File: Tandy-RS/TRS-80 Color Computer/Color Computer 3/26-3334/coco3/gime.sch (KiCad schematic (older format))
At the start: 28 parts, among them IC10 74LS244, IC11 74LS244, IC12 74LS244, IC13 74LS374, IC15 74LS04, IC6 TCC1014, IC9 74LS138, X1 Crystal

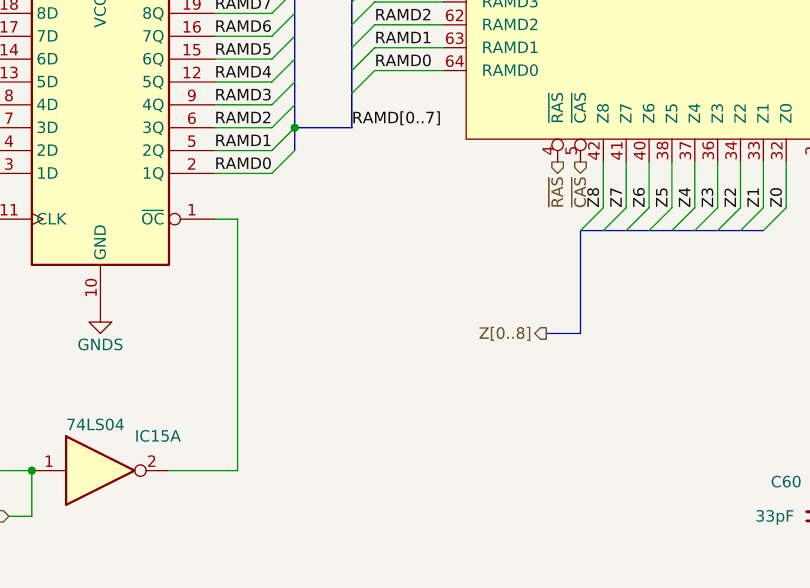
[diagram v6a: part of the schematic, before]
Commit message: found and added lost capacitor c68
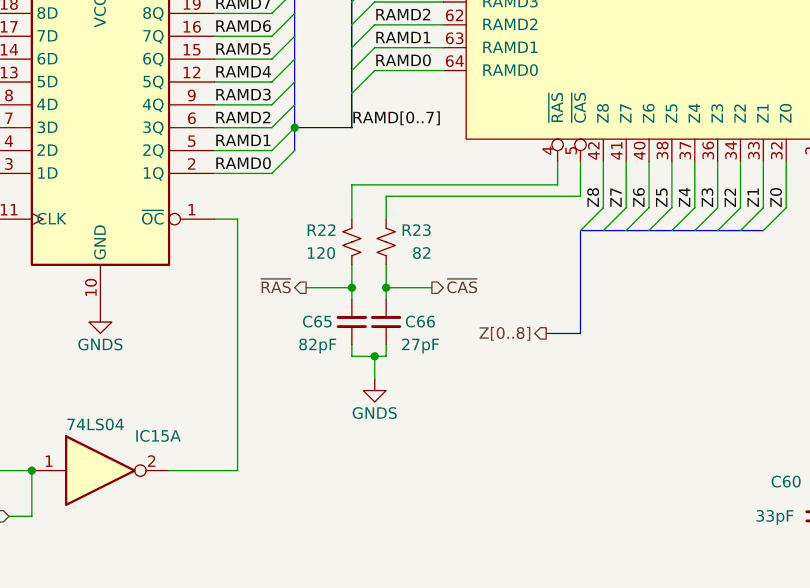
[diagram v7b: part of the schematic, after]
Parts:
- added C65: 82pF, Capacitor_THT:C_Rect_L7.2mm_W3.0mm_P5.00mm_FKS2_FKP2_MKS2_MKP2, symbol Device:C_Small
- added C66: 27pF, Capacitor_THT:C_Rect_L7.2mm_W3.0mm_P5.00mm_FKS2_FKP2_MKS2_MKP2, symbol Device:C_Small
- added R22: 120, Resistor_THT:R_Axial_DIN0207_L6.3mm_D2.5mm_P10.16mm_Horizontal, symbol Device:R_Small_US
- added R23: 82, Resistor_THT:R_Axial_DIN0207_L6.3mm_D2.5mm_P10.16mm_Horizontal, symbol Device:R_Small_US
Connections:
- net GNDS: now also C65.1, C66.1
- net ~CAS: now also C66.2, R23.1; no longer IC6.5 (~CAS)
- net ~RAS: now also C65.2, R22.1; no longer IC6.4 (~RAS)
- new net: IC6.4 (~RAS), R22.2
- new net: IC6.5 (~CAS), R23.2
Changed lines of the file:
@@
 Wire Wire Line
 	4150 6750 4450 6750
-Text HLabel 6850 5400 3    50   Output ~ 0
+Text HLabel 6200 5950 2    50   Output ~ 0
 ~CAS
-Text HLabel 6750 5400 3    50   Output ~ 0
+Text HLabel 5650 5950 0    50   Output ~ 0
 ~RAS
 Text HLabel 4350 6950 0    50   Input ~ 0
@@
 Text Label 6000 4000 0    50   ~ 0
 ~WE1
-Wire Bus Line
-	1950 2200 1950 5950
-Wire Bus Line
-	6100 2150 8050 2150
-Wire Bus Line
-	5900 850  5900 3500
-Wire Bus Line
-	6850 5700 7650 5700
-Wire Bus Line
-	3900 4850 3900 6950
-Wire Bus Line
-	3650 4850 3650 6950
-Wire Bus Line
-	3900 850  3900 2700
-Wire Bus Line
-	3650 850  3650 2700
-Wire Bus Line
-	5850 4400 5850 5250
-Wire Bus Line
-	5600 2200 5600 5250
 Text HLabel 5900 4000 0    50   Output ~ 0
 ~WE1
+$Comp
+L Device:R_Small_US R?
+U 1 1 612F6A83
+P 5850 5750
+AR Path="/60273794/612F6A83" Ref="R?"  Part="1"
+AR Path="/603D560B/612F6A83" Ref="R?"  Part="1"
+AR Path="/603CF7B8/612F6A83" Ref="R?"  Part="1"
+AR Path="/612A4892/612F6A83" Ref="R?"  Part="1"
+AR Path="/61257512/612F6A83" Ref="R22"  Part="1"
+F 0 "R22" H 5650 5700 50  0000 L CNN
+F 1 " 120" H 5650 5800 50  0000 L CNN
+F 2 "Resistor_THT:R_Axial_DIN0207_L6.3mm_D2.5mm_P10.16mm_Horizontal" H 5850 5750 50  0001 C CNN
+F 3 " https://www.seielect.com/catalog/sei-cf_cfm.pdf" H 5850 5750 50  0001 C CNN
+F 4 "digikey" H 5850 5750 50  0001 C CNN "Vendor"
+F 5 "CF14JT120RCT-ND" H 5850 5750 50  0001 C CNN "Vendor part#"
+F 6 "CF14JT120R" H 5850 5750 50  0001 C CNN "Manufacturer part#"
+	1    5850 5750
+	1    0    0    1
+$EndComp
+Wire Wire Line
+	6750 5400 6750 5500
+Wire Wire Line
+	6750 5500 5850 5500
+Wire Wire Line
+	5850 5500 5850 5650
+$Comp
+L Device:R_Small_US R?
+U 1 1 61342388
+P 6000 5750
+AR Path="/60273794/61342388" Ref="R?"  Part="1"
+AR Path="/603D560B/61342388" Ref="R?"  Part="1"
+AR Path="/603CF7B8/61342388" Ref="R?"  Part="1"
+AR Path="/612A4892/61342388" Ref="R?"  Part="1"
+AR Path="/61257512/61342388" Ref="R23"  Part="1"
+F 0 "R23" H 5800 5700 50  0000 L CNN
+F 1 "82" H 5800 5800 50  0000 L CNN
+F 2 "Resistor_THT:R_Axial_DIN0207_L6.3mm_D2.5mm_P10.16mm_Horizontal" H 6000 5750 50  0001 C CNN
+F 3 "https://www.koaspeer.com/pdfs/CF.pdf" H 6000 5750 50  0001 C CNN
+F 4 "digikey" H 6000 5750 50  0001 C CNN "Vendor"
+F 5 "2019-CF1/4CT52R820JCT-ND" H 6000 5750 50  0001 C CNN "Vendor part#"
+F 6 "CF1/4CT52R820J" H 6000 5750 50  0001 C CNN "Manufacturer part#"
+	1    6000 5750
+	-1   0    0    1
+$EndComp
+Wire Wire Line
+	6850 5400 6850 5550
+Wire Wire Line
+	6850 5550 6000 5550
+Wire Wire Line
+	6000 5550 6000 5650
+$Comp
+L Device:C_Small C?
+U 1 1 6136F6EC
+P 6000 6100
+AR Path="/60273794/6136F6EC" Ref="C?"  Part="1"
+AR Path="/602A51A8/6136F6EC" Ref="C?"  Part="1"
+AR Path="/603CF7B8/6136F6EC" Ref="C?"  Part="1"
+AR Path="/61257512/6136F6EC" Ref="C66"  Part="1"
+F 0 "C66" H 5850 6100 50  0000 C CNN
+F 1 "27pF" H 5850 6200 50  0000 C CNN
+F 2 "Capacitor_THT:C_Rect_L7.2mm_W3.0mm_P5.00mm_FKS2_FKP2_MKS2_MKP2" H 6000 6100 50  0001 C CNN
+F 3 "https://www.vishay.com/docs/45171/kseries.pdf" H 6000 6100 50  0001 C CNN
+F 4 "digikey" V 6000 6100 50  0001 C CNN "Vendor"
+F 5 "BC1035CT-ND" V 6000 6100 50  0001 C CNN "Vendor part#"
+F 6 "K270J15C0GF5TH5" V 6000 6100 50  0001 C CNN "Manufacturer part#"
+	1    6000 6100
+	-1   0    0    1
+$EndComp
+$Comp
+L Device:C_Small C?
+U 1 1 6138ACD5
+P 5850 6100
+AR Path="/60273794/6138ACD5" Ref="C?"  Part="1"
+AR Path="/602A51A8/6138ACD5" Ref="C?"  Part="1"
+AR Path="/603CF7B8/6138ACD5" Ref="C?"  Part="1"
+AR Path="/61257512/6138ACD5" Ref="C65"  Part="1"
+F 0 "C65" H 5700 6100 50  0000 C CNN
+F 1 "82pF" H 5700 6200 50  0000 C CNN
+F 2 "Capacitor_THT:C_Rect_L7.2mm_W3.0mm_P5.00mm_FKS2_FKP2_MKS2_MKP2" H 5850 6100 50  0001 C CNN
+F 3 "https://www.vishay.com/docs/45171/kseries.pdf" H 5850 6100 50  0001 C CNN
+F 4 "digikey" V 5850 6100 50  0001 C CNN "Vendor"
+F 5 "BC1041CT-ND" V 5850 6100 50  0001 C CNN "Vendor part#"
+F 6 "K820J15C0GF5TH5" V 5850 6100 50  0001 C CNN "Manufacturer part#"
+	1    5850 6100
+	1    0    0    1
+$EndComp
+$Comp
+L power:GNDS #PWR?
+U 1 1 6138FA4F
+P 5950 6350
+AR Path="/602A51A8/6138FA4F" Ref="#PWR?"  Part="1"
+AR Path="/60308A73/6138FA4F" Ref="#PWR?"  Part="1"
+AR Path="/603E4732/6138FA4F" Ref="#PWR?"  Part="1"
+AR Path="/603D345E/6138FA4F" Ref="#PWR?"  Part="1"
+AR Path="/6138FA4F" Ref="#PWR?"  Part="1"
+AR Path="/61257512/6138FA4F" Ref="#PWR0101"  Part="1"
+F 0 "#PWR0101" H 5950 6100 50  0001 C CNN
+F 1 "GNDS" H 5950 6200 50  0000 C CNN
+F 2 "" H 5950 6350 50  0001 C CNN
+F 3 "" H 5950 6350 50  0001 C CNN
+	1    5950 6350
+	-1   0    0    -1
+$EndComp
+Wire Wire Line
+	5850 6200 5850 6250
+Wire Wire Line
+	5850 6250 5950 6250
+Wire Wire Line
+	5950 6250 5950 6350
+Wire Wire Line
+	6000 6200 6000 6250
+Wire Wire Line
+	6000 6250 5950 6250
+Connection ~ 5950 6250
+Wire Wire Line
+	6000 5850 6000 5950
+Wire Wire Line
+	5850 5850 5850 5950
+Wire Wire Line
+	5650 5950 5850 5950
+Connection ~ 5850 5950
+Wire Wire Line
+	5850 5950 5850 6000
+Wire Wire Line
+	6200 5950 6000 5950
+Connection ~ 6000 5950
+Wire Wire Line
+	6000 5950 6000 6000
+Wire Bus Line
+	3650 4850 3650 6950
+Wire Bus Line
+	3900 4850 3900 6950
+Wire Bus Line
+	5900 850  5900 3500
+Wire Bus Line
+	6850 5700 7650 5700
+Wire Bus Line
+	3900 850  3900 2700
+Wire Bus Line
+	3650 850  3650 2700
+Wire Bus Line
+	5850 4400 5850 5250
+Wire Bus Line
+	5600 2200 5600 5250
+Wire Bus Line
+	1950 2200 1950 5950
+Wire Bus Line
+	6100 2150 8050 2150
 $EndSCHEMATC

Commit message: -swapped 5v to 8v inthe video section. -swapped collector and emitter connections for Q1 -sourced more coponents -started pcb
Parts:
- IC6: footprint (none) -> Package_LCC:PLCC-68_THT-Socket; Manufacturer part# (none) -> Assmann WSW Components; Vendor (none) -> digikey; Vendor part# (none) -> AE11249-ND
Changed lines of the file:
@@
 F 0 "IC6" H 7800 4300 50  0000 L CNN
 F 1 "TCC1014" H 7650 4150 50  0000 L CNN
-F 2 "" H 7850 4150 50  0001 C CNN
-F 3 "" H 7850 4150 50  0001 C CNN
+F 2 "Package_LCC:PLCC-68_THT-Socket" H 7850 4150 50  0001 C CNN
+F 3 "http://www.assmann-wsw.com/uploads/datasheets/ASS_7007_CO.pdf" H 7850 4150 50  0001 C CNN
+F 4 "digikey" H 7800 3950 50  0001 C CNN "Vendor"
+F 5 "AE11249-ND" H 7800 3950 50  0001 C CNN "Vendor part#"
+F 6 "Assmann WSW Components" H 7800 3950 50  0001 C CNN "Manufacturer part#"
 	1    7800 3950
 	1    0    0    -1
